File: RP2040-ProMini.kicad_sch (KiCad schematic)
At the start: 36 parts, among them J1 CONN_L, J2 CONN_U, J3 CONN_R2, J4 CONN_R, Q1 AO3400A, U1 W25Q128JVS, U2 RP2040, U3 MIC5205-3.3YM5, U4 W25Q128JVEIQ, Y1 12MHz

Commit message: Added buck-boost converter TPS63060 instead of LDO
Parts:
- removed C1: 2.2uF, Capacitor_SMD:C_0603_1608Metric, symbol Device:C_Small
- removed U3: MIC5205-3.3YM5, Package_TO_SOT_SMD:SOT-23-5, symbol Regulator_Linear:MIC5205-3.3YM5
- added C15: 100nF, Capacitor_SMD:C_0402_1005Metric, symbol Device:C_Small
- added L1: 1.5uH, Inductor_SMD:L_Murata_DFE201610P, symbol Device:L_Small
- added R10: 174k, Resistor_SMD:R_0402_1005Metric, symbol Device:R_Small
- added R8, R9: 1M, Resistor_SMD:R_0402_1005Metric, symbol Device:R_Small
- added U3: TPS63060, Package_SON:Texas_S-PWSON-N10_ThermalVias, symbol Regulator_Switching:TPS63060
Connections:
- net GND: now also C15.2, R10.1, U3.11 (PGND), U3.4 (PS/SYNC), U3.7 (GND)
- net VIN: now also U3.2 (VIN), U3.3 (EN)
- net VOUT: now reaches D2.2 (A), JP2.1 (A)
- net VOUT: now also R8.2, R9.2, U3.9 (VOUT)
- new net: R8.1, U3.5 (PG)
- new net: C15.1, U3.6 (VAUX)
- new net FB: R10.2, R9.1, U3.8 (FB)
- new net L1: L1.1, U3.1 (L1)
- new net L2: L1.2, U3.10 (L2)
- no-connect marks 11 -> 10
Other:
- note added: "Buck-boost power supply"
- note added: "Vout = Vfb * (R1 + R2) / R2 Vout = 0.5V * (1M + 174k) /1 174k Vout = 3.37V"
- note removed: "LDO power supply"
- title: RP2040-ProMini-0011 -> RP2040-ProMini-0020
- moved on the sheet: C12, C14, D2, JP2, R6

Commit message: Added D20 and D21. Fixed minor issues. Moved stuff around.
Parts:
- added J5: CONN_R3, Connector_PinHeader_2.54mm:PinHeader_1x02_P2.54mm_Vertical, symbol Connector_Generic:Conn_01x02
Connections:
- net D20: now reaches U2.34 (GPIO22)
- net D20: now also J5.1 (Pin_1)
- net D21: now reaches U2.35 (GPIO23)
- net D21: now also J5.2 (Pin_2)
- no-connect marks 10 -> 8
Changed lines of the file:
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@@
   (junction (at 151.13 39.37) (diameter 0) (color 0 0 0 0)
   )
-  (no_connect (at 166.37 102.87))
   (no_connect (at 166.37 54.61))
   (no_connect (at 166.37 52.07))
@@
   (no_connect (at 166.37 67.31))
   (no_connect (at 166.37 107.95))
-  (no_connect (at 166.37 105.41))
   (wire (pts (xy 233.68 130.81) (xy 242.57 130.81))
     (stroke (width 0) (type default))
@@
     )
   )
+  (global_label "D20" (shape input) (at 231.14 79.375 90) (fields_autoplaced)
+    (effects (font (size 1.27 1.27)) (justify left))
+    (property "Intersheetrefs" "${INTERSHEET_REFS}" (at 231.14 72.7802 90)
+      (effects (font (size 1.27 1.27)) (justify left) hide)
+    )
+  )
   (global_label "QSPI_SD3" (shape input) (at 31.75 99.06 180) (fields_autoplaced)
     (effects (font (size 1.27 1.27)) (justify right))
@@
     )
   )
+  (global_label "D20" (shape input) (at 166.37 102.87 0) (fields_autoplaced)
+    (effects (font (size 1.27 1.27)) (justify left))
+    (property "Intersheetrefs" "${INTERSHEET_REFS}" (at 172.9648 102.87 0)
+      (effects (font (size 1.27 1.27)) (justify left) hide)
+    )
+  )
   (global_label "VIN" (shape input) (at 254 55.88 0) (fields_autoplaced)
     (effects (font (size 1.27 1.27)) (justify left))
@@
     )
   )
+  (global_label "D21" (shape input) (at 166.37 105.41 0) (fields_autoplaced)
+    (effects (font (size 1.27 1.27)) (justify left))
+    (property "Intersheetrefs" "${INTERSHEET_REFS}" (at 172.9648 105.41 0)
+      (effects (font (size 1.27 1.27)) (justify left) hide)
+    )
+  )
   (global_label "D0_RX" (shape input) (at 203.2 58.42 180) (fields_autoplaced)
     (effects (font (size 1.27 1.27)) (justify right))
@@
     (effects (font (size 1.27 1.27)) (justify left))
     (property "Intersheetrefs" "${INTERSHEET_REFS}" (at 171.7553 97.79 0)
+      (effects (font (size 1.27 1.27)) (justify left) hide)
+    )
+  )
+  (global_label "D21" (shape input) (at 233.68 79.375 90) (fields_autoplaced)
+    (effects (font (size 1.27 1.27)) (justify left))
+    (property "Intersheetrefs" "${INTERSHEET_REFS}" (at 233.68 72.7802 90)
       (effects (font (size 1.27 1.27)) (justify left) hide)
     )
@@
         )
       )
+    )
+  )
+  (symbol (lib_id "Connector_Generic:Conn_01x02") (at 231.14 84.455 90) (mirror x) (unit 1)
+    (in_bom yes) (on_board yes) (dnp no)
+    (property "Reference" "J5" (at 236.855 83.185 90)
+      (effects (font (size 1.27 1.27)) (justify right))
+    )
+    (property "Value" "CONN_R3" (at 236.855 85.725 90)
+      (effects (font (size 1.27 1.27)) (justify right))
+    )
+    (property "Footprint" "Connector_PinHeader_2.54mm:PinHeader_1x02_P2.54mm_Vertical" (at 231.14 84.455 0)
+      (effects (font (size 1.27 1.27)) hide)
+    )
+    (property "Datasheet" "~" (at 231.14 84.455 0)
+      (effects (font (size 1.27 1.27)) hide)
+    )
+    (pin "1")
+    (pin "2")
+    (instances
+      (project "RP2040-ProMini"
+        (path "/9a38a81c-7302-494f-9784-2ab4342a0a1d"
+          (reference "J5") (unit 1)
+        )
+      )

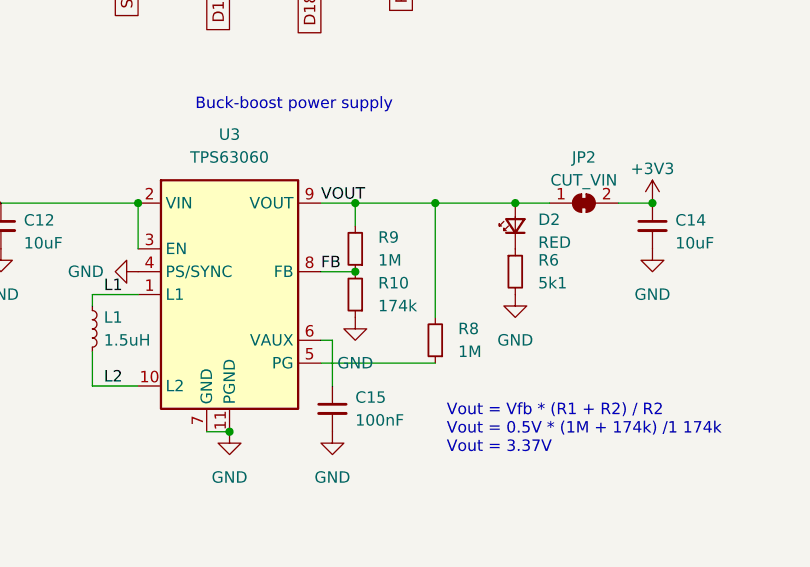
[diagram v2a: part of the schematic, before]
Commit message: Moved few traces around.
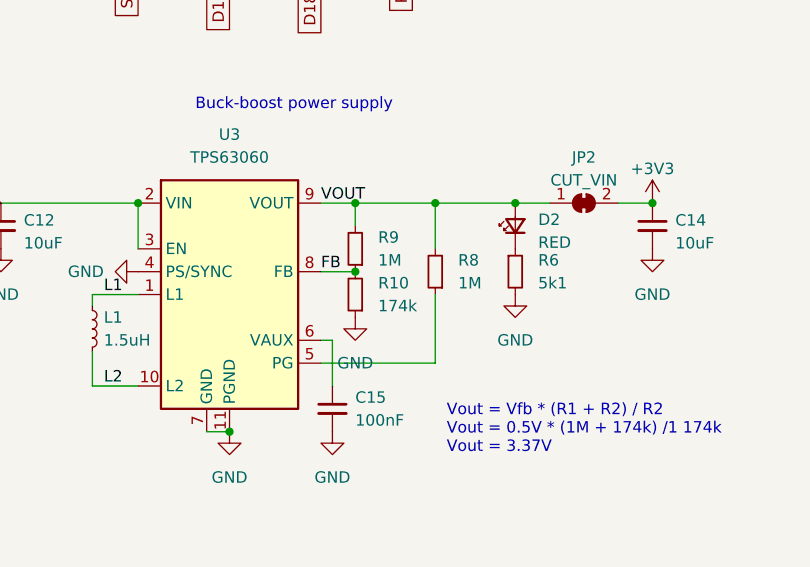
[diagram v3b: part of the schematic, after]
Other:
- moved on the sheet: R8
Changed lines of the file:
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@@
   (title_block
     (title "RP2040-ProMini-0020")
-    (date "2023-07-09")
+    (date "2023-07-10")
     (rev "2.0")
     (company "(c) 2023 Andriy Golovnya")
@@
     (stroke (width 0) (type default))
   )
-  (wire (pts (xy 242.57 130.81) (xy 242.57 143.51))
+  (wire (pts (xy 242.57 130.81) (xy 242.57 135.89))
     (stroke (width 0) (type default))
   )
@@
     (stroke (width 0) (type default))
   )
+  (wire (pts (xy 242.57 140.97) (xy 242.57 148.59))
+    (stroke (width 0) (type default))
+  )
   (wire (pts (xy 135.89 39.37) (xy 138.43 39.37))
     (stroke (width 0) (type default))
   )
-  (wire (pts (xy 229.87 148.59) (xy 242.57 148.59))
-    (stroke (width 0) (type default))
-  )
   (wire (pts (xy 148.59 39.37) (xy 151.13 39.37))
     (stroke (width 0) (type default))
@@
   )
   (wire (pts (xy 251.46 130.81) (xy 255.27 130.81))
+    (stroke (width 0) (type default))
+  )
+  (wire (pts (xy 242.57 148.59) (xy 229.87 148.59))
     (stroke (width 0) (type default))
   )
@@
     )
   )
-  (symbol (lib_id "Device:R_Small") (at 242.57 146.05 180) (unit 1)
-    (in_bom yes) (on_board yes) (dnp no) (fields_autoplaced)
-    (property "Reference" "R8" (at 245.11 144.78 0)
+  (symbol (lib_id "Device:R_Small") (at 242.57 138.43 180) (unit 1)
+    (in_bom yes) (on_board yes) (dnp no) (fields_autoplaced)
+    (property "Reference" "R8" (at 245.11 137.16 0)
       (effects (font (size 1.27 1.27)) (justify right))
     )
-    (property "Value" "1M" (at 245.11 147.32 0)
+    (property "Value" "1M" (at 245.11 139.7 0)
       (effects (font (size 1.27 1.27)) (justify right))
     )
-    (property "Footprint" "Resistor_SMD:R_0402_1005Metric" (at 242.57 146.05 0)
-      (effects (font (size 1.27 1.27)) hide)
-    )
-    (property "Datasheet" "~" (at 242.57 146.05 0)
-      (effects (font (size 1.27 1.27)) hide)
-    )
+    (property "Footprint" "Resistor_SMD:R_0402_1005Metric" (at 242.57 138.43 0)
+      (effects (font (size 1.27 1.27)) hide)
+    )
+    (property "Datasheet" "~" (at 242.57 138.43 0)
+      (effects (font (size 1.27 1.27)) hide)
+    )

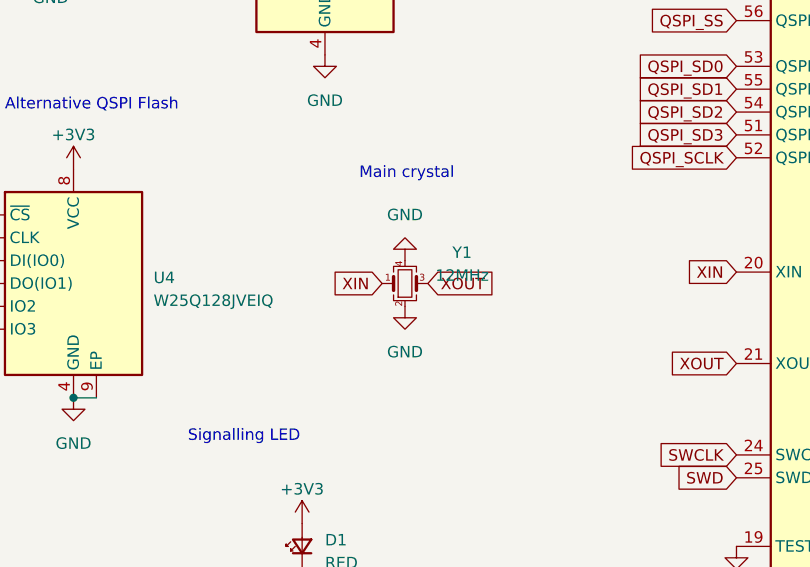
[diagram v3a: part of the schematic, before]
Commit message: Rotated quartz for better silk markings alignment
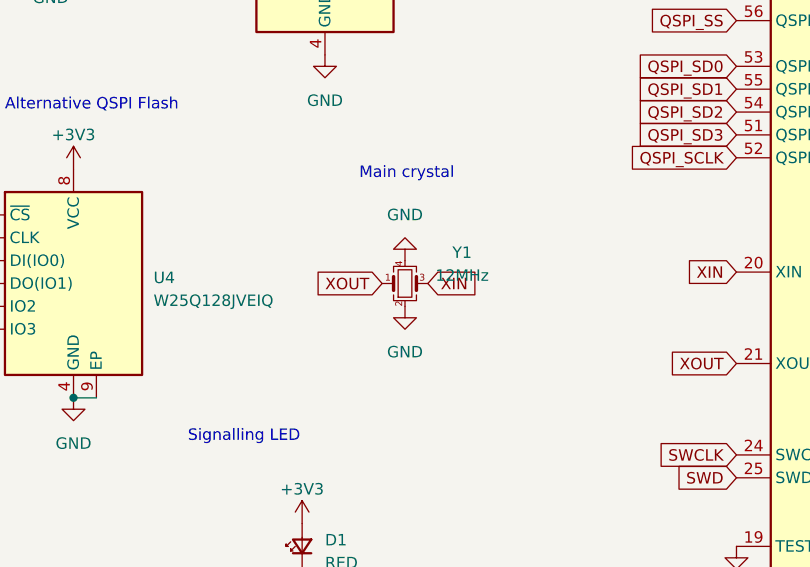
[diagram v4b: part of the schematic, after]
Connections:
- net XIN: now also Y1.3; no longer Y1.1
- net XOUT: now also Y1.1; no longer Y1.3
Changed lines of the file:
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@@
     )
   )
-  (global_label "XIN" (shape input) (at 76.2 93.98 180) (fields_autoplaced)
-    (effects (font (size 1.27 1.27)) (justify right))
-    (property "Intersheetrefs" "${INTERSHEET_REFS}" (at 70.1494 93.98 0)
-      (effects (font (size 1.27 1.27)) (justify right) hide)
+  (global_label "XIN" (shape input) (at 81.28 93.98 0) (fields_autoplaced)
+    (effects (font (size 1.27 1.27)) (justify left))
+    (property "Intersheetrefs" "${INTERSHEET_REFS}" (at 87.3306 93.98 0)
+      (effects (font (size 1.27 1.27)) (justify left) hide)
     )
   )
@@
     )
   )
-  (global_label "XOUT" (shape input) (at 81.28 93.98 0) (fields_autoplaced)
-    (effects (font (size 1.27 1.27)) (justify left))
-    (property "Intersheetrefs" "${INTERSHEET_REFS}" (at 89.0239 93.98 0)
-      (effects (font (size 1.27 1.27)) (justify left) hide)
+  (global_label "XOUT" (shape input) (at 76.2 93.98 180) (fields_autoplaced)
+    (effects (font (size 1.27 1.27)) (justify right))
+    (property "Intersheetrefs" "${INTERSHEET_REFS}" (at 68.4561 93.98 0)
+      (effects (font (size 1.27 1.27)) (justify right) hide)
     )
   )

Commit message: Adjusted few texts
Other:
- note added: "Vout = Vfb * (R1 + R2) / R2 Vout = 0.5V * (1M + 174k) / 174k Vout = 3.37V"
- note removed: "Vout = Vfb * (R1 + R2) / R2 Vout = 0.5V * (1M + 174k) /1 174k Vout = 3.37V"
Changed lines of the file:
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@@
   (title_block
     (title "RP2040-ProMini-0020")
-    (date "2023-07-10")
+    (date "2023-07-13")
     (rev "2.0")
     (company "(c) 2023 Andriy Golovnya")
@@
     (effects (font (size 1.27 1.27)) (justify left bottom))
   )
-  (text "Vout = Vfb * (R1 + R2) / R2\nVout = 0.5V * (1M + 174k) /1 174k\nVout = 3.37V"
+  (text "Vout = Vfb * (R1 + R2) / R2\nVout = 0.5V * (1M + 174k) / 174k\nVout = 3.37V"
     (at 243.84 158.75 0)
     (effects (font (size 1.27 1.27)) (justify left bottom))

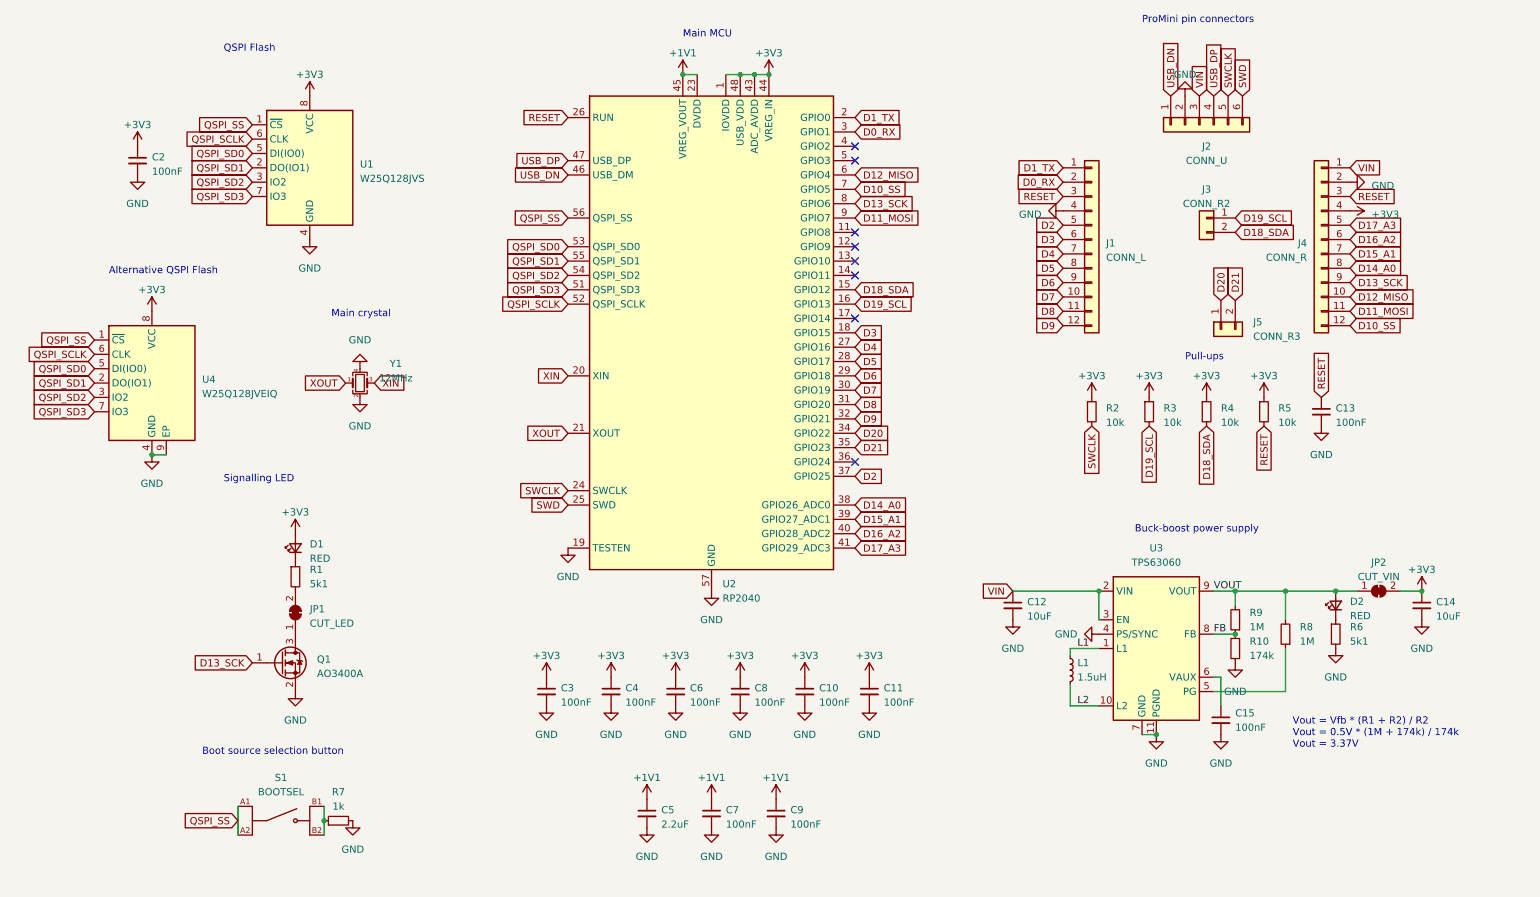
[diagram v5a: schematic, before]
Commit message: Moved few stuff around. Added storage cap.
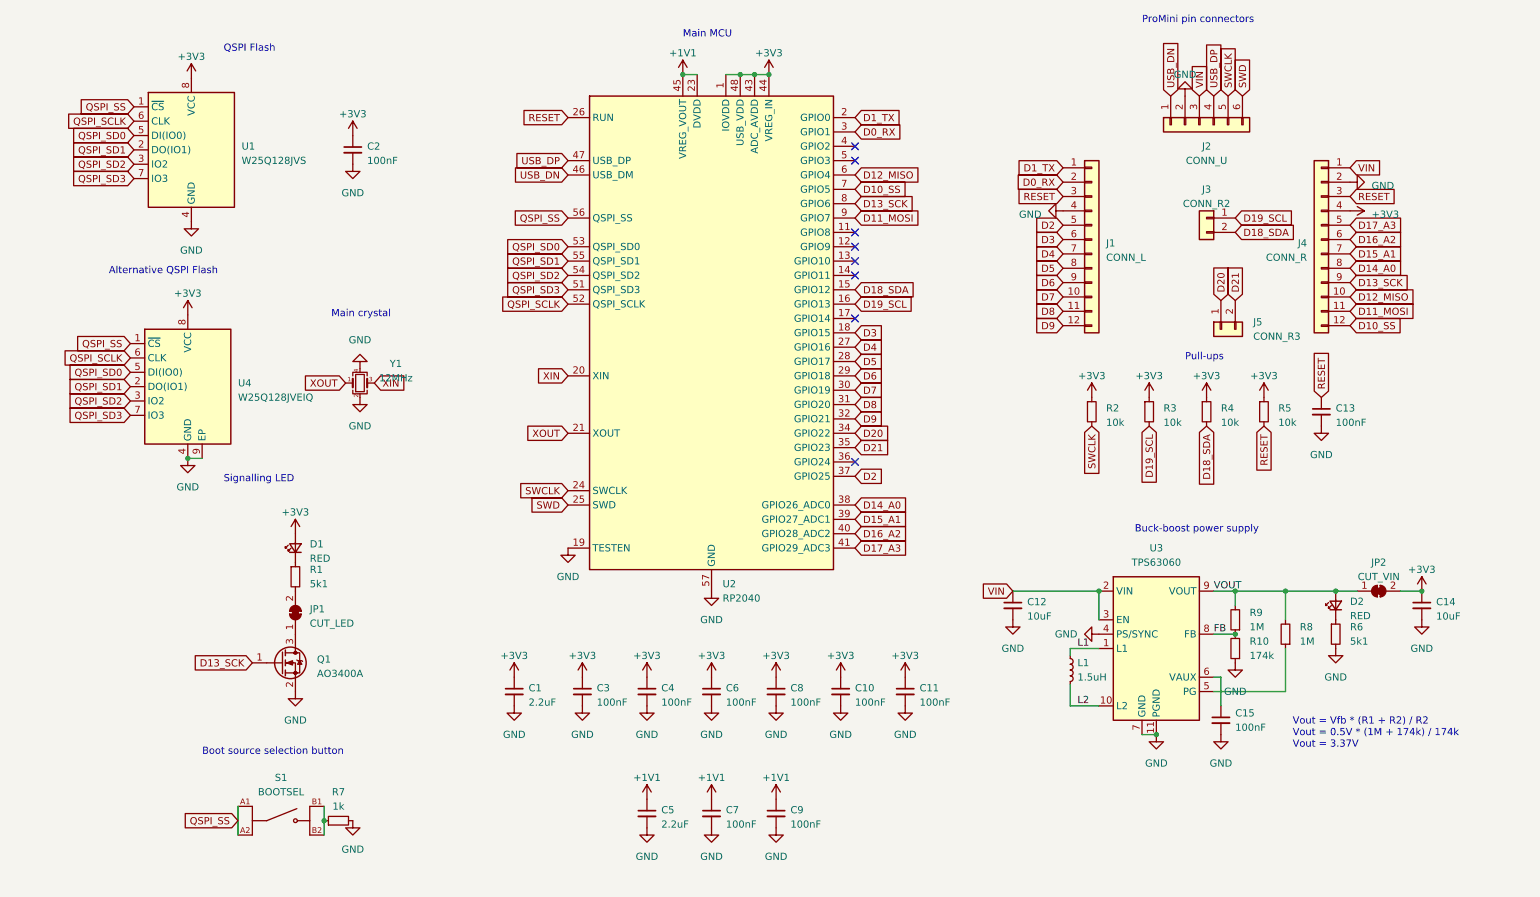
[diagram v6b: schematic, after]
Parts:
- added C1: 2.2uF, Capacitor_SMD:C_0603_1608Metric, symbol Device:C_Small
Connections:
- net +3V3: now also C1.1
- net GND: now also C1.2
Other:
- moved on the sheet: C10, C11, C2, C3, C4, C6, C8, U1, U4

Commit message: Added few descriptive texts on schematics
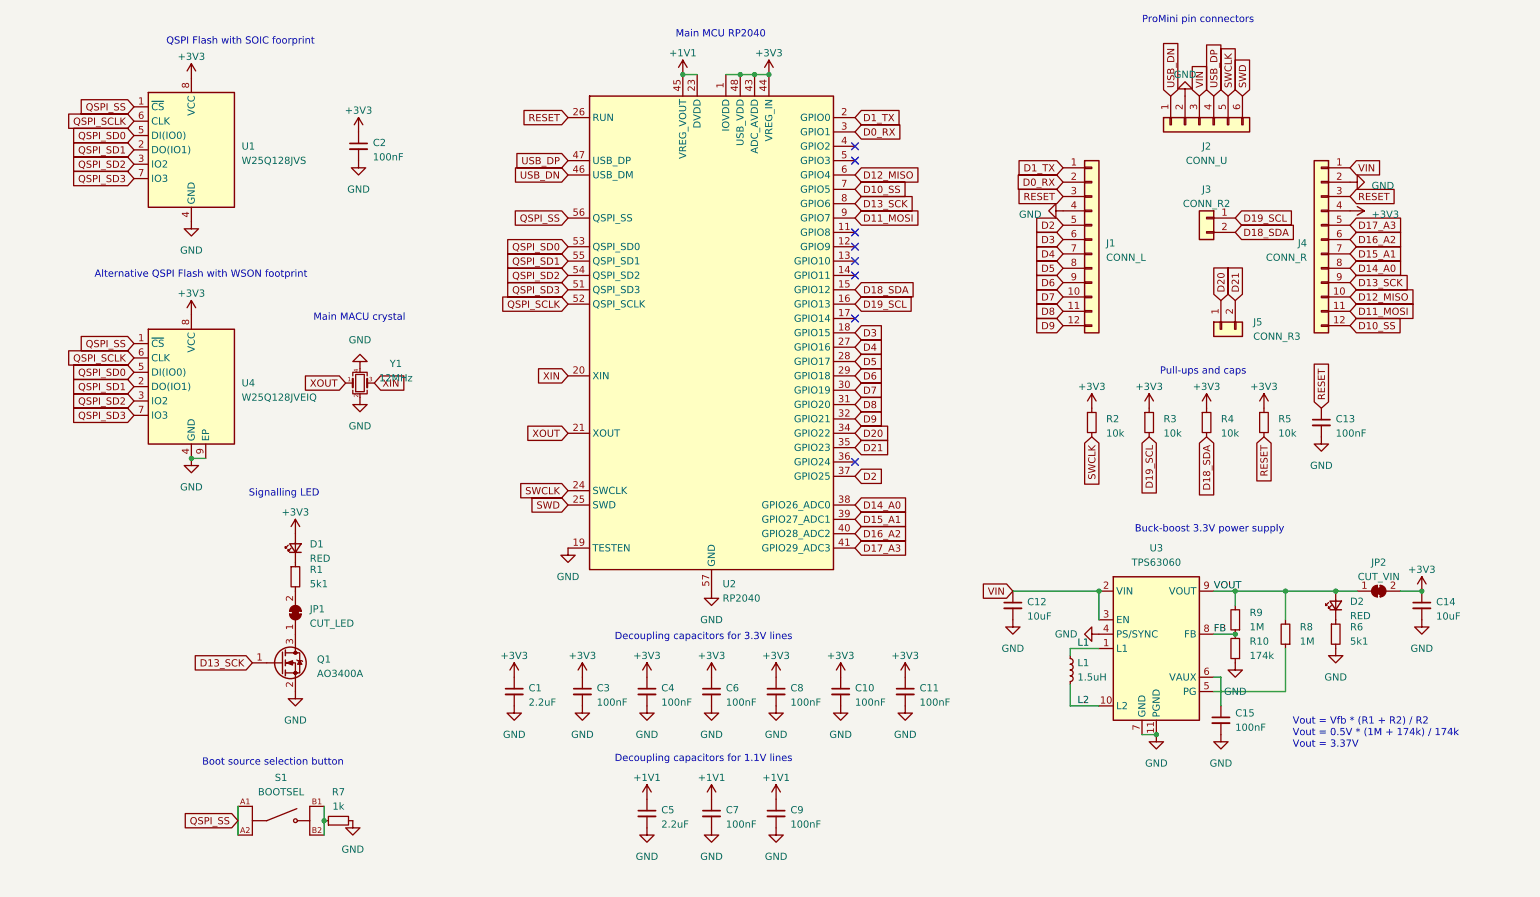
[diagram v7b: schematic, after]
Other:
- note added: "Alternative QSPI Flash with WSON footprint"
- note added: "Buck-boost 3.3V power supply"
- note added: "Decoupling capacitors for 1.1V lines"
- note added: "Decoupling capacitors for 3.3V lines"
- note added: "Main MACU crystal"
- note added: "Main MCU RP2040"
- note added: "Pull-ups and caps"
- note added: "QSPI Flash with SOIC foorprint"
- note removed: "Alternative QSPI Flash"
- note removed: "Buck-boost power supply"
- note removed: "Main MCU"
- note removed: "Main crystal"
- note removed: "Pull-ups"
- note removed: "QSPI Flash"
- moved on the sheet: C13, C2, R2, R3, R4, R5, U4
